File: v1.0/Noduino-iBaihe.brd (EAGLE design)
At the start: 68.6 x 53.3 mm, 42 parts, among them IC1 5V, Q1 SI2302, Q2 SI2302, Q3 SI2302, Q4 SI2302, Q5 SI2302

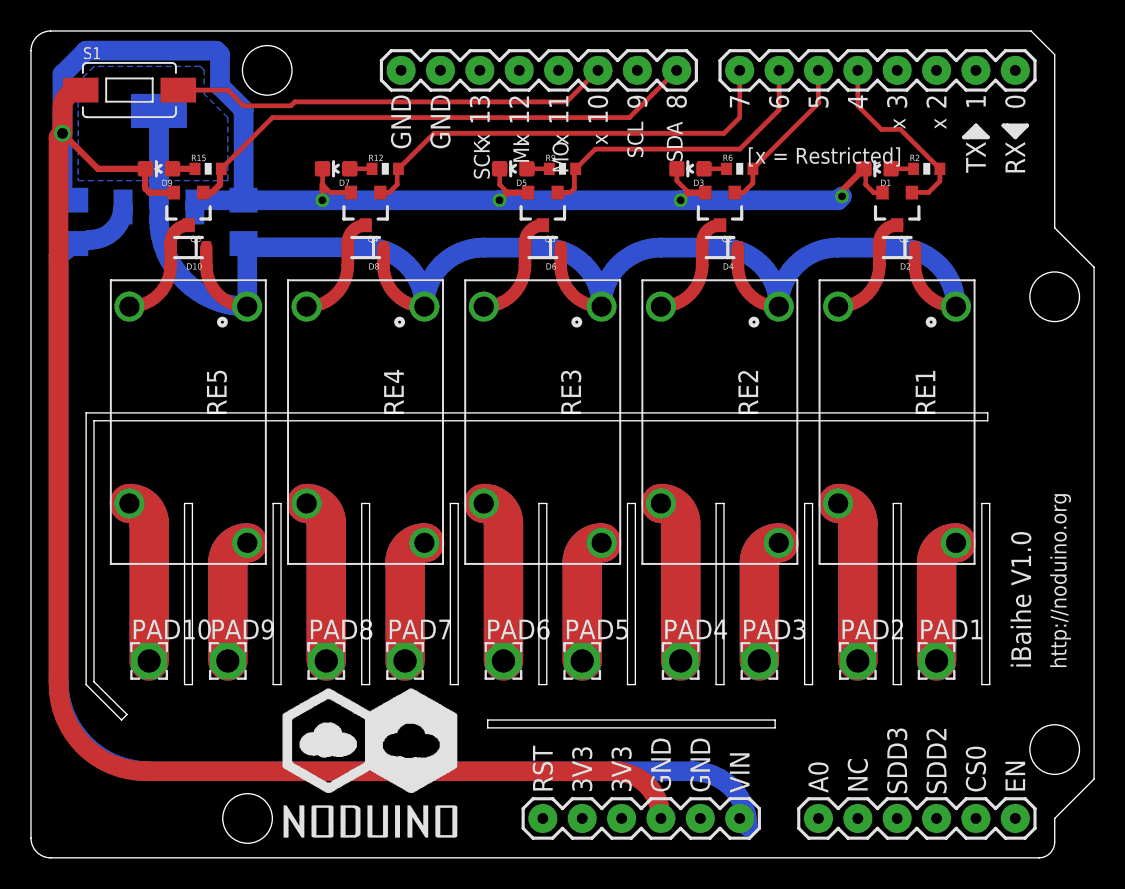
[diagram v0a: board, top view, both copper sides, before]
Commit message: change the drill size of pins interface to 0.9mm
The old drill size of v1.0 shield is 0.7mm.
It's too small
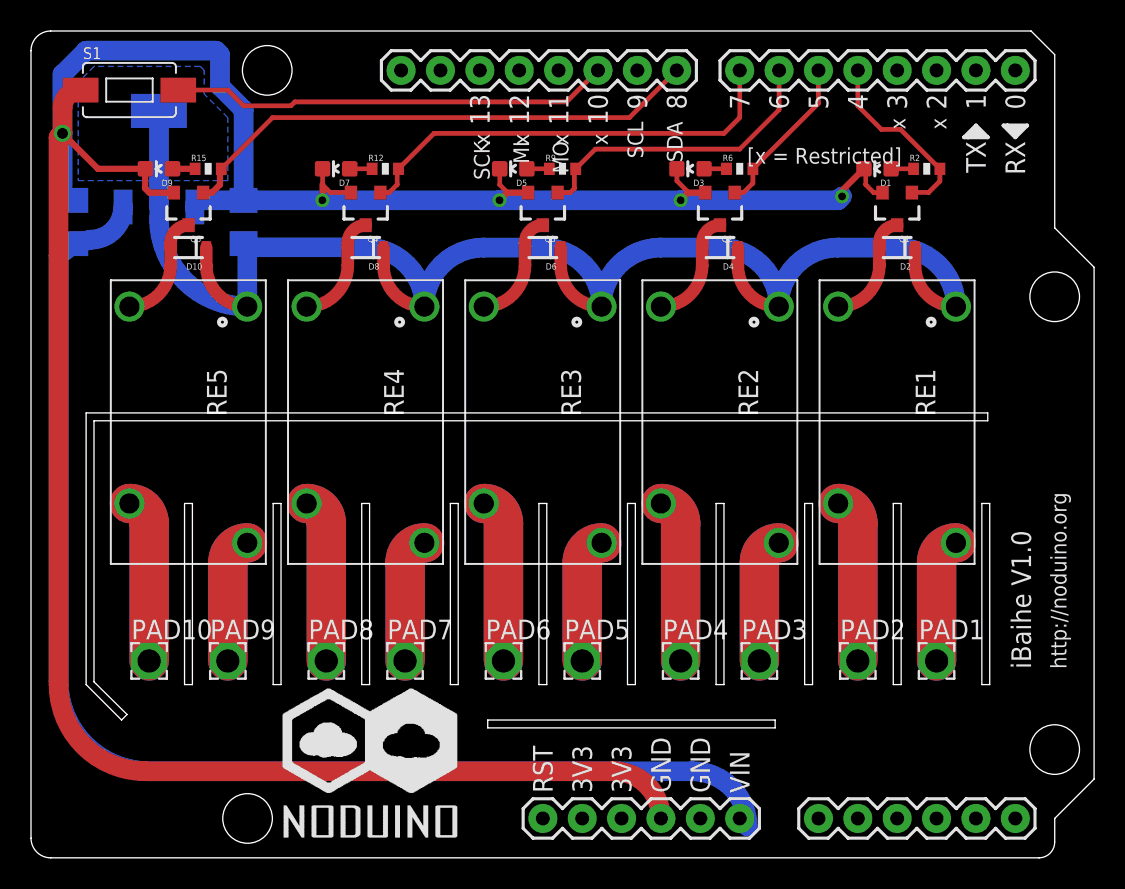
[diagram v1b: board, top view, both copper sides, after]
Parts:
- N1: value NODUINO-PIN -> NODUINO-PINMAIL; device ehl:NODUINO-PIN -> ehl:NODUINO-PIN-MAIL
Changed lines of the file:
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@@
 <element name="PAD9" library="ehl" package="2,15/1,0" value="" x="12.7" y="12.7"/>
 <element name="PAD10" library="ehl" package="2,15/1,0" value="" x="7.62" y="12.7"/>
-<element name="N1" library="ehl" package="NODUINO-PIN" value="NODUINO-PIN" x="0" y="0"/>
+<element name="N1" library="ehl" package="NODUINO-PIN-MAIL" value="NODUINO-PINMAIL" x="0" y="0"/>
 <element name="IC1" library="ehl" package="SOT223" value="5V" x="8.255" y="45.085" rot="MR0"/>
 <element name="C1" library="ehl" package="C1206" value="22uF" x="2.794" y="41.021" rot="MR90"/>
